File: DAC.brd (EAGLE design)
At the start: 81.3 x 76.2 mm, 89 parts, among them IC1 LM2662, IC2 PCM1793, IC3 OPA2134PA, IC4 LMH6643, J1 USBSMD, J2 RCJ-21XXMILL, U1 LDO-TPS78233, U2 PCM2707, Y1 12MHz/20pF

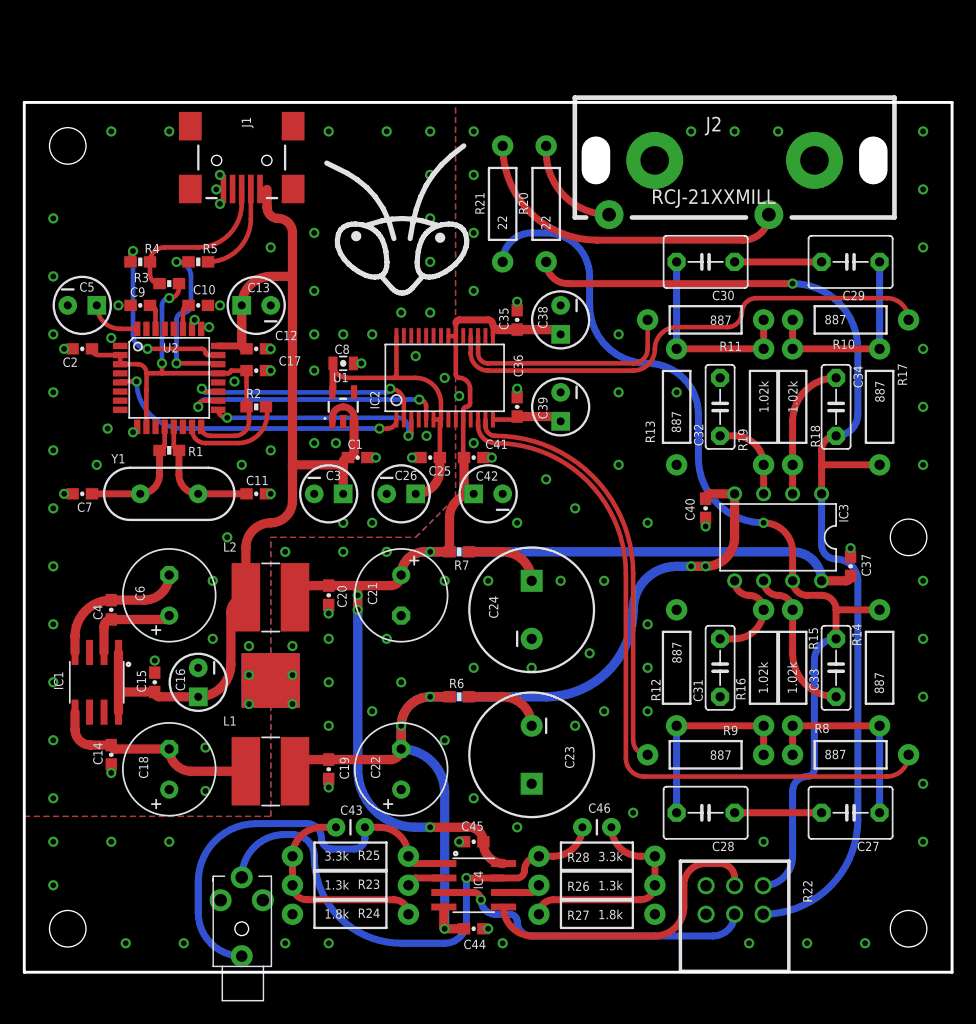
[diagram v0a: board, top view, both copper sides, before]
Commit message: 2.5mm jack was placed by mistake
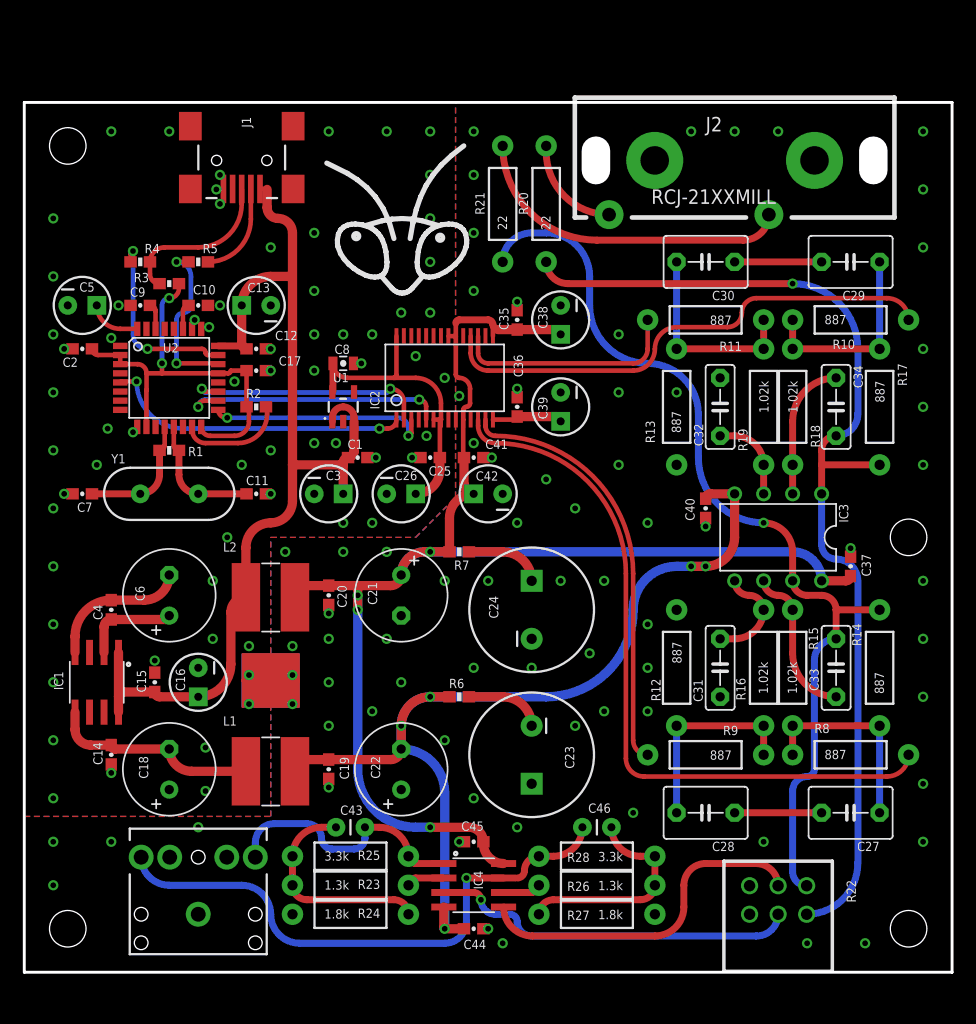
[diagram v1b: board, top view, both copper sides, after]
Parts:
- J3: device SparkFun-Connectors:STEREOJACK2.5MM_STEREOJACK2.5MM -> SparkFun-Connectors:AUDIO-JACK
- moved J3 4.02 mm to (15.2, 5.08)
- moved R22 3.81 mm to (66.0, 5.08)
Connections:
- net AGND: now also J3.SLEEVE; no longer J3.RING1
- net HP_L: now also J3.TIP; no longer J3.SHIELD
- net HP_R: now also J3.RING; no longer J3.TIP
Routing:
- net HP_L: track 35.3 -> 22.1 mm
- net HP_R: track 41.8 -> 48.2 mm
- net N$12: track 27.8 -> 31.7 mm
- net N$15: track 26.2 -> 29.7 mm
- net OUT_L*: track 91.1 -> 89.6 mm
- net OUT_R*: track 79.8 -> 79.2 mm
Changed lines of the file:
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@@
 <attribute name="NAME" x="39.37" y="8.89" size="0.8128" layer="25" ratio="15" rot="R270"/>
 </element>
-<element name="R22" library="my" package="PTD902" value="TD90" x="62.23" y="5.08" smashed="yes" rot="R270">
-<attribute name="NAME" x="68.23" y="8.08" size="0.8128" layer="25" font="vector" ratio="15" rot="R270"/>
-<attribute name="VALUE" x="55.23" y="8.08" size="1.27" layer="27" font="vector" rot="R270"/>
+<element name="R22" library="my" package="PTD902" value="TD90" x="66.04" y="5.08" smashed="yes" rot="R270">
+<attribute name="NAME" x="72.04" y="8.08" size="0.8128" layer="25" font="vector" ratio="15" rot="R270"/>
+<attribute name="VALUE" x="59.04" y="8.08" size="1.27" layer="27" font="vector" rot="R270"/>
 </element>
 <element name="R25" library="SparkFun-Resistors" package="AXIAL-0.4" value="3.3k" x="28.575" y="10.16" smashed="yes">
@@
 <attribute name="VALUE" x="29.591" y="14.224" size="0.4064" layer="27" rot="R180"/>
 </element>
-<element name="J3" library="SparkFun-Connectors" package="STEREOJACK2.5MM_STEREOJACK2.5MM" value="" x="19.05" y="3.81" smashed="yes" rot="R90"/>
+<element name="J3" library="SparkFun-Connectors" package="AUDIO-JACK" value="" x="15.24" y="5.08" smashed="yes" rot="R90"/>
 <element name="R28" library="SparkFun-Resistors" package="AXIAL-0.4" value="3.3k" x="50.165" y="10.16" smashed="yes" rot="R180">
 <attribute name="NAME" x="49.53" y="10.4775" size="0.8128" layer="25" font="vector" ratio="15" rot="R180"/>
@@
 <contactref element="R22" pad="R1.1"/>
 <contactref element="R24" pad="P$1"/>
-<contactref element="J3" pad="RING1"/>
+<contactref element="J3" pad="SLEEVE"/>
 <contactref element="R27" pad="P$1"/>
 <contactref element="R22" pad="R2.1"/>
@@
 <via x="73.66" y="2.54" extent="1-16" drill="0.5"/>
 <via x="68.58" y="2.54" extent="1-16" drill="0.5"/>
-<via x="63.5" y="2.54" extent="1-16" drill="0.5"/>
 <via x="41.91" y="2.54" extent="1-16" drill="0.5"/>
 <via x="53.34" y="13.97" extent="1-16" drill="0.5"/>
@@
 <via x="39.37" y="15.24" extent="1-16" drill="0.5"/>
 <via x="36.83" y="20.32" extent="1-16" drill="0.5"/>
-<via x="22.86" y="2.54" extent="1-16" drill="0.5"/>
-<via x="26.67" y="2.54" extent="1-16" drill="0.5"/>
-<via x="13.97" y="2.54" extent="1-16" drill="0.5"/>
-<via x="8.89" y="2.54" extent="1-16" drill="0.5"/>
 <via x="2.54" y="7.62" extent="1-16" drill="0.5"/>
 <via x="2.54" y="11.43" extent="1-16" drill="0.5"/>
 <via x="7.62" y="11.43" extent="1-16" drill="0.5"/>
-<via x="12.7" y="11.43" extent="1-16" drill="0.5"/>
+<via x="15.24" y="12.7" extent="1-16" drill="0.5"/>
 <via x="64.77" y="11.43" extent="1-16" drill="0.5"/>
 </signal>
@@
 <wire x1="74.93" y1="44.45" x2="69.85" y2="44.45" width="0.6096" layer="1"/>
 <contactref element="R22" pad="R1.3"/>
-<wire x1="64.73" y1="5.08" x2="73.025" y2="13.375" width="0.6096" layer="16" curve="90"/>
-<wire x1="73.025" y1="13.375" x2="73.025" y2="34.29" width="0.6096" layer="16"/>
+<wire x1="73.025" y1="9.565" x2="73.025" y2="34.29" width="0.6096" layer="16"/>
 <wire x1="73.025" y1="34.29" x2="71.12" y2="36.195" width="0.6096" layer="16" curve="90"/>
 <wire x1="71.12" y1="36.195" x2="69.85" y2="37.465" width="0.6096" layer="16" curve="-90"/>
@@
 <wire x1="73.025" y1="54.61" x2="73.025" y2="48.895" width="0.6096" layer="16"/>
 <wire x1="73.025" y1="48.895" x2="71.12" y2="46.99" width="0.6096" layer="16" curve="-90"/>
+<wire x1="73.025" y1="9.565" x2="68.54" y2="5.08" width="0.6096" layer="16" curve="-90"/>
 </signal>
 <signal name="OUT_R*" class="2">
@@
 <wire x1="69.215" y1="17.78" x2="69.215" y2="27.305" width="0.6096" layer="16"/>
 <wire x1="69.215" y1="27.305" x2="71.12" y2="29.21" width="0.6096" layer="16" curve="-90"/>
-<wire x1="64.73" y1="7.58" x2="67.31" y2="10.16" width="0.6096" layer="16" curve="90"/>
-<wire x1="67.31" y1="10.16" x2="67.31" y2="15.875" width="0.6096" layer="16"/>
 <wire x1="67.31" y1="15.875" x2="68.58" y2="17.145" width="0.6096" layer="16" curve="-90"/>
 <wire x1="67.31" y1="34.29" x2="67.31" y2="36.83" width="0.6096" layer="1"/>
@@
 <wire x1="45.72" y1="64.77" x2="44.45" y2="64.77" width="0.6096" layer="16"/>
 <wire x1="44.45" y1="64.77" x2="41.91" y2="62.23" width="0.6096" layer="16" curve="90"/>
+<wire x1="67.31" y1="15.875" x2="67.31" y2="8.81" width="0.6096" layer="16"/>
+<wire x1="67.31" y1="8.81" x2="68.54" y2="7.58" width="0.6096" layer="16" curve="90"/>
 </signal>
 <signal name="N$12" class="2">
@@
 <wire x1="42.545" y1="5.08" x2="43.18" y2="4.445" width="0.6096" layer="16" curve="-90"/>
 <wire x1="43.18" y1="4.445" x2="44.45" y2="3.175" width="0.6096" layer="16" curve="90"/>
-<wire x1="44.45" y1="3.175" x2="60.325" y2="3.175" width="0.6096" layer="16"/>
-<wire x1="60.325" y1="3.175" x2="62.23" y2="5.08" width="0.6096" layer="16" curve="90"/>
+<wire x1="44.45" y1="3.175" x2="64.135" y2="3.175" width="0.6096" layer="16"/>
+<wire x1="64.135" y1="3.175" x2="66.04" y2="5.08" width="0.6096" layer="16" curve="90"/>
 </signal>
 <signal name="HP_L" class="2">
@@
 <contactref element="R25" pad="P$2"/>
 <contactref element="C43" pad="1"/>
-<contactref element="J3" pad="SHIELD"/>
+<contactref element="J3" pad="TIP"/>
 <wire x1="36.7538" y1="9.525" x2="34.29" y2="9.525" width="0.6096" layer="1"/>
 <wire x1="34.29" y1="9.525" x2="33.655" y2="10.16" width="0.6096" layer="1" curve="-90"/>
 <wire x1="33.655" y1="10.16" x2="31.115" y2="12.7" width="0.6096" layer="1" curve="90"/>
 <wire x1="31.115" y1="12.7" x2="29.845" y2="12.7" width="0.6096" layer="1"/>
-<wire x1="19.05" y1="1.41" x2="15.24" y2="5.22" width="0.6096" layer="16" curve="-90"/>
-<wire x1="15.24" y1="5.22" x2="15.24" y2="7.9375" width="0.6096" layer="16"/>
-<wire x1="15.24" y1="7.9375" x2="20.32" y2="13.0175" width="0.6096" layer="16" curve="-90"/>
-<wire x1="20.32" y1="13.0175" x2="24.765" y2="13.0175" width="0.6096" layer="16"/>
 <wire x1="24.765" y1="13.0175" x2="26.035" y2="11.7475" width="0.6096" layer="16" curve="-90"/>
 <wire x1="26.035" y1="11.7475" x2="26.9875" y2="10.795" width="0.6096" layer="16" curve="90"/>
@@
 <wire x1="28.8925" y1="10.795" x2="29.845" y2="11.7475" width="0.6096" layer="16" curve="90"/>
 <wire x1="29.845" y1="11.7475" x2="29.845" y2="12.7" width="0.6096" layer="16"/>
+<wire x1="24.765" y1="13.0175" x2="21.9075" y2="13.0175" width="0.6096" layer="16"/>
+<wire x1="21.9075" y1="13.0175" x2="20.24" y2="11.35" width="0.6096" layer="16" curve="90"/>
+<wire x1="20.24" y1="11.35" x2="20.24" y2="10.08" width="0.6096" layer="16"/>
 </signal>
 <signal name="N$14" class="2">
@@
 </signal>
 <signal name="HP_R" class="2">
-<contactref element="J3" pad="TIP"/>
+<contactref element="J3" pad="RING"/>
 <contactref element="R28" pad="P$2"/>
 <contactref element="C46" pad="1"/>
@@
 <wire x1="38.735" y1="8.255" x2="38.735" y2="4.445" width="0.6096" layer="16"/>
 <wire x1="38.735" y1="4.445" x2="36.83" y2="2.54" width="0.6096" layer="16" curve="-90"/>
-<wire x1="36.83" y1="2.54" x2="33.02" y2="2.54" width="0.6096" layer="16"/>
 <wire x1="41.9862" y1="8.255" x2="43.18" y2="8.255" width="0.4064" layer="1"/>
 <wire x1="43.18" y1="8.255" x2="43.815" y2="8.89" width="0.6096" layer="1" curve="90"/>
@@
 <wire x1="45.085" y1="10.16" x2="46.355" y2="10.16" width="0.6096" layer="1"/>
 <wire x1="46.355" y1="10.16" x2="48.895" y2="12.7" width="0.6096" layer="1" curve="90"/>
-<wire x1="33.02" y1="2.54" x2="25.4" y2="10.16" width="0.6096" layer="16" curve="-90"/>
-<wire x1="25.4" y1="10.16" x2="23.495" y2="12.065" width="0.6096" layer="16" curve="90"/>
-<wire x1="23.495" y1="12.065" x2="22.805" y2="12.065" width="0.6096" layer="16"/>
-<wire x1="22.805" y1="12.065" x2="19.05" y2="8.31" width="0.6096" layer="16" curve="90"/>
+<wire x1="12.7" y1="7.62" x2="10.24" y2="10.08" width="0.6096" layer="16" curve="-90"/>
+<wire x1="12.7" y1="7.62" x2="19.05" y2="7.62" width="0.6096" layer="16"/>
+<wire x1="19.05" y1="7.62" x2="21.59" y2="5.08" width="0.6096" layer="16" curve="-90"/>
+<wire x1="21.59" y1="5.08" x2="24.13" y2="2.54" width="0.6096" layer="16" curve="90"/>
+<wire x1="24.13" y1="2.54" x2="36.83" y2="2.54" width="0.6096" layer="16"/>
 </signal>
 <signal name="N$19" class="2">
@@
 <wire x1="57.785" y1="5.715" x2="57.785" y2="7.62" width="0.6096" layer="1"/>
 <wire x1="57.785" y1="7.62" x2="59.69" y2="9.525" width="0.6096" layer="1" curve="-90"/>
-<wire x1="59.69" y1="9.525" x2="60.96" y2="9.525" width="0.6096" layer="1"/>
-<wire x1="60.96" y1="9.525" x2="62.23" y2="8.255" width="0.6096" layer="1" curve="-90"/>
-<wire x1="62.23" y1="8.255" x2="62.23" y2="7.58" width="0.6096" layer="1"/>
+<wire x1="59.69" y1="9.525" x2="64.095" y2="9.525" width="0.6096" layer="1"/>
+<wire x1="64.095" y1="9.525" x2="66.04" y2="7.58" width="0.6096" layer="1" curve="-90"/>
 </signal>
 <signal name="N$6" class="2">

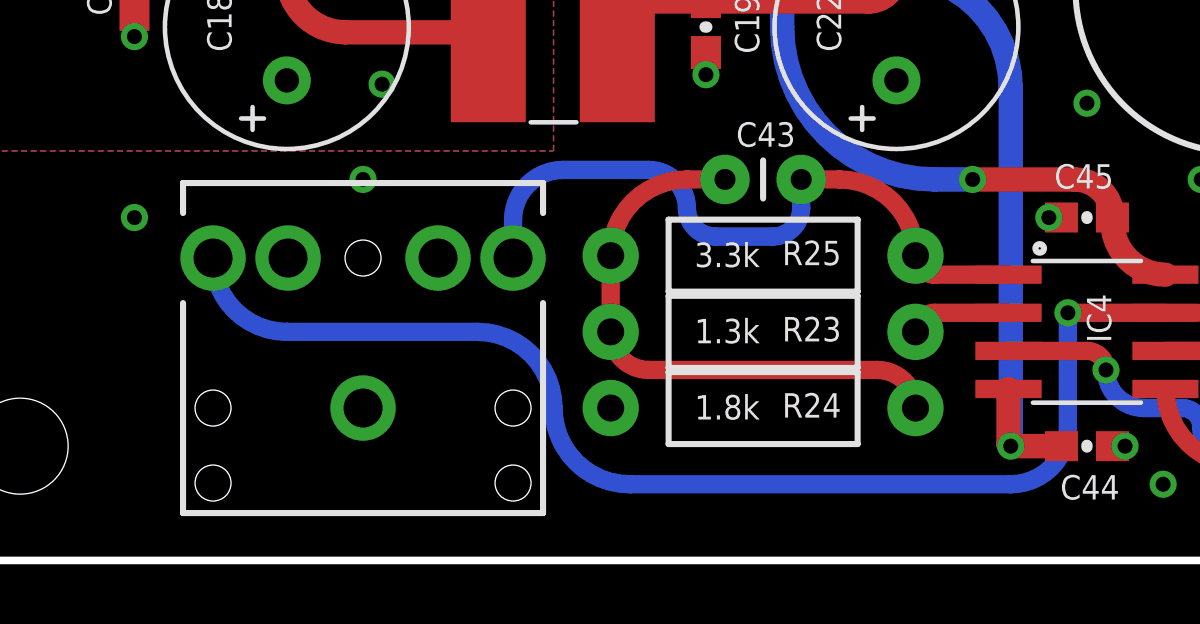
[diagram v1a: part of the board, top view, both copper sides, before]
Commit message: Phone jack position adjusted
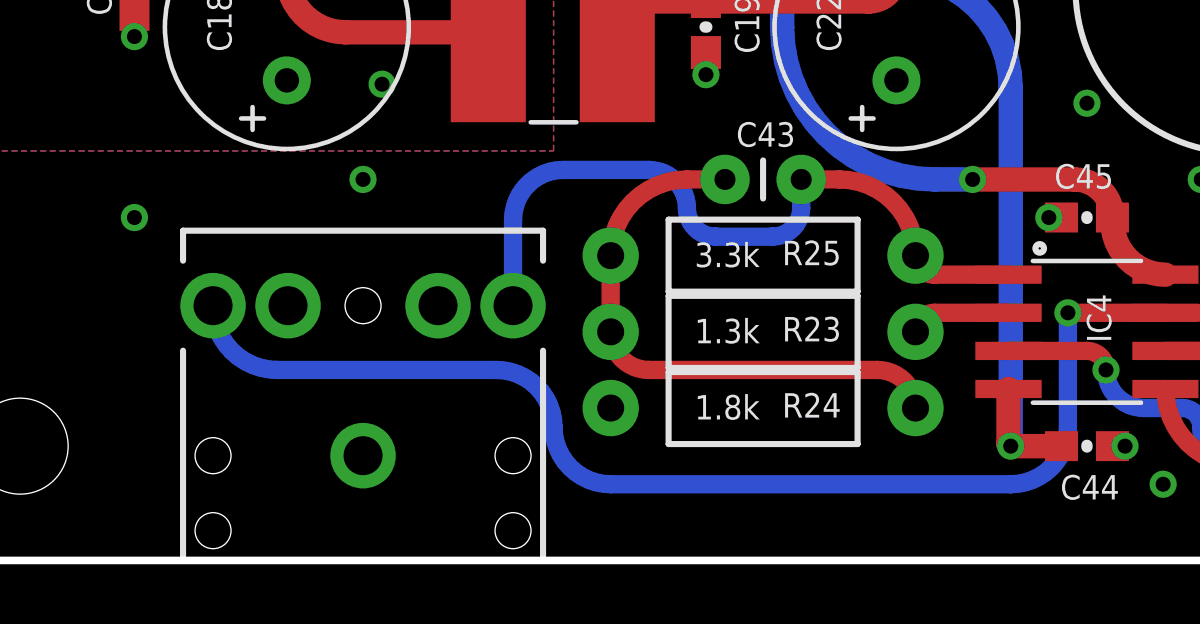
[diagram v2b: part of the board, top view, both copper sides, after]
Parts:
- moved J3 1.59 mm to (15.2, 3.49)
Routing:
- net HP_L: track 22.1 -> 23.6 mm
- net HP_R: track 48.2 -> 47.6 mm
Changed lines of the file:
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@@
 <attribute name="VALUE" x="29.591" y="14.224" size="0.4064" layer="27" rot="R180"/>
 </element>
-<element name="J3" library="SparkFun-Connectors" package="AUDIO-JACK" value="" x="15.24" y="5.08" smashed="yes" rot="R90"/>
+<element name="J3" library="SparkFun-Connectors" package="AUDIO-JACK" value="" x="15.24" y="3.4925" smashed="yes" rot="R90"/>
 <element name="R28" library="SparkFun-Resistors" package="AXIAL-0.4" value="3.3k" x="50.165" y="10.16" smashed="yes" rot="R180">
 <attribute name="NAME" x="49.53" y="10.4775" size="0.8128" layer="25" font="vector" ratio="15" rot="R180"/>
@@
 <wire x1="24.765" y1="13.0175" x2="21.9075" y2="13.0175" width="0.6096" layer="16"/>
 <wire x1="21.9075" y1="13.0175" x2="20.24" y2="11.35" width="0.6096" layer="16" curve="90"/>
-<wire x1="20.24" y1="11.35" x2="20.24" y2="10.08" width="0.6096" layer="16"/>
+<wire x1="20.24" y1="11.35" x2="20.24" y2="8.4925" width="0.6096" layer="16"/>
 </signal>
 <signal name="N$14" class="2">
@@
 <wire x1="45.085" y1="10.16" x2="46.355" y2="10.16" width="0.6096" layer="1"/>
 <wire x1="46.355" y1="10.16" x2="48.895" y2="12.7" width="0.6096" layer="1" curve="90"/>
-<wire x1="12.7" y1="7.62" x2="10.24" y2="10.08" width="0.6096" layer="16" curve="-90"/>
-<wire x1="12.7" y1="7.62" x2="19.05" y2="7.62" width="0.6096" layer="16"/>
-<wire x1="19.05" y1="7.62" x2="21.59" y2="5.08" width="0.6096" layer="16" curve="-90"/>
-<wire x1="21.59" y1="5.08" x2="24.13" y2="2.54" width="0.6096" layer="16" curve="90"/>
-<wire x1="24.13" y1="2.54" x2="36.83" y2="2.54" width="0.6096" layer="16"/>
+<wire x1="23.495" y1="2.54" x2="36.83" y2="2.54" width="0.6096" layer="16"/>
+<wire x1="10.24" y1="8.4925" x2="12.3825" y2="6.35" width="0.6096" layer="16" curve="90"/>
+<wire x1="12.3825" y1="6.35" x2="19.685" y2="6.35" width="0.6096" layer="16"/>
+<wire x1="19.685" y1="6.35" x2="21.59" y2="4.445" width="0.6096" layer="16" curve="-90"/>
+<wire x1="21.59" y1="4.445" x2="23.495" y2="2.54" width="0.6096" layer="16" curve="90"/>
 </signal>
 <signal name="N$19" class="2">
